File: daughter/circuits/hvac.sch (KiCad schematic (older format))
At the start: 60 parts, among them Q1 Q_MBT3904, Q10 BC846, Q11 BSS84, Q12 BSS84, Q13 Q_MBT3904, Q14 Q_MBT3904, Q15 Q_DMT3020, Q16 Q_DMT3020, Q2 Q_MBT3904, Q3 Q_DMT3020, Q4 Q_DMT3020, Q5 Q_MBT3904, Q6 Q_MBT3904, Q7 Q_DMT3020, Q8 Q_DMT3020, Q9 BC846, U10 MAX11617, U11 LTV-827S, U9 MCP23017_SS

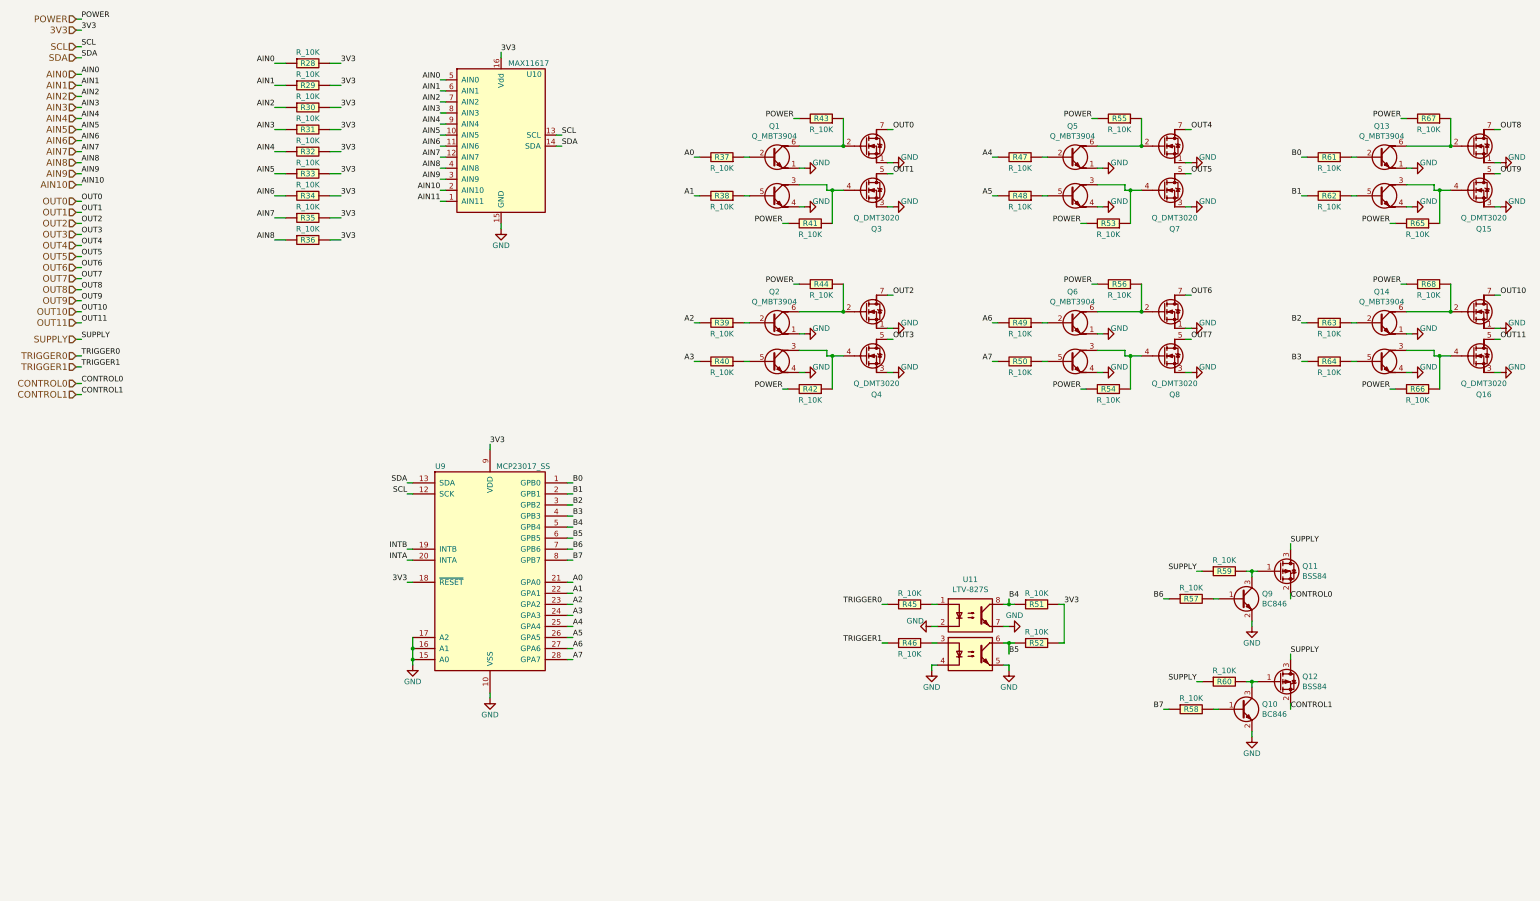
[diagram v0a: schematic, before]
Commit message: 0) Switched to h-bridge drivers for hvac 1) Connected ignition sense io 2) MCP config pins and reset 3) Fixed usb resistors 4) Fixed BJT footprint 5) Added car interface pcb for C6 Corvette
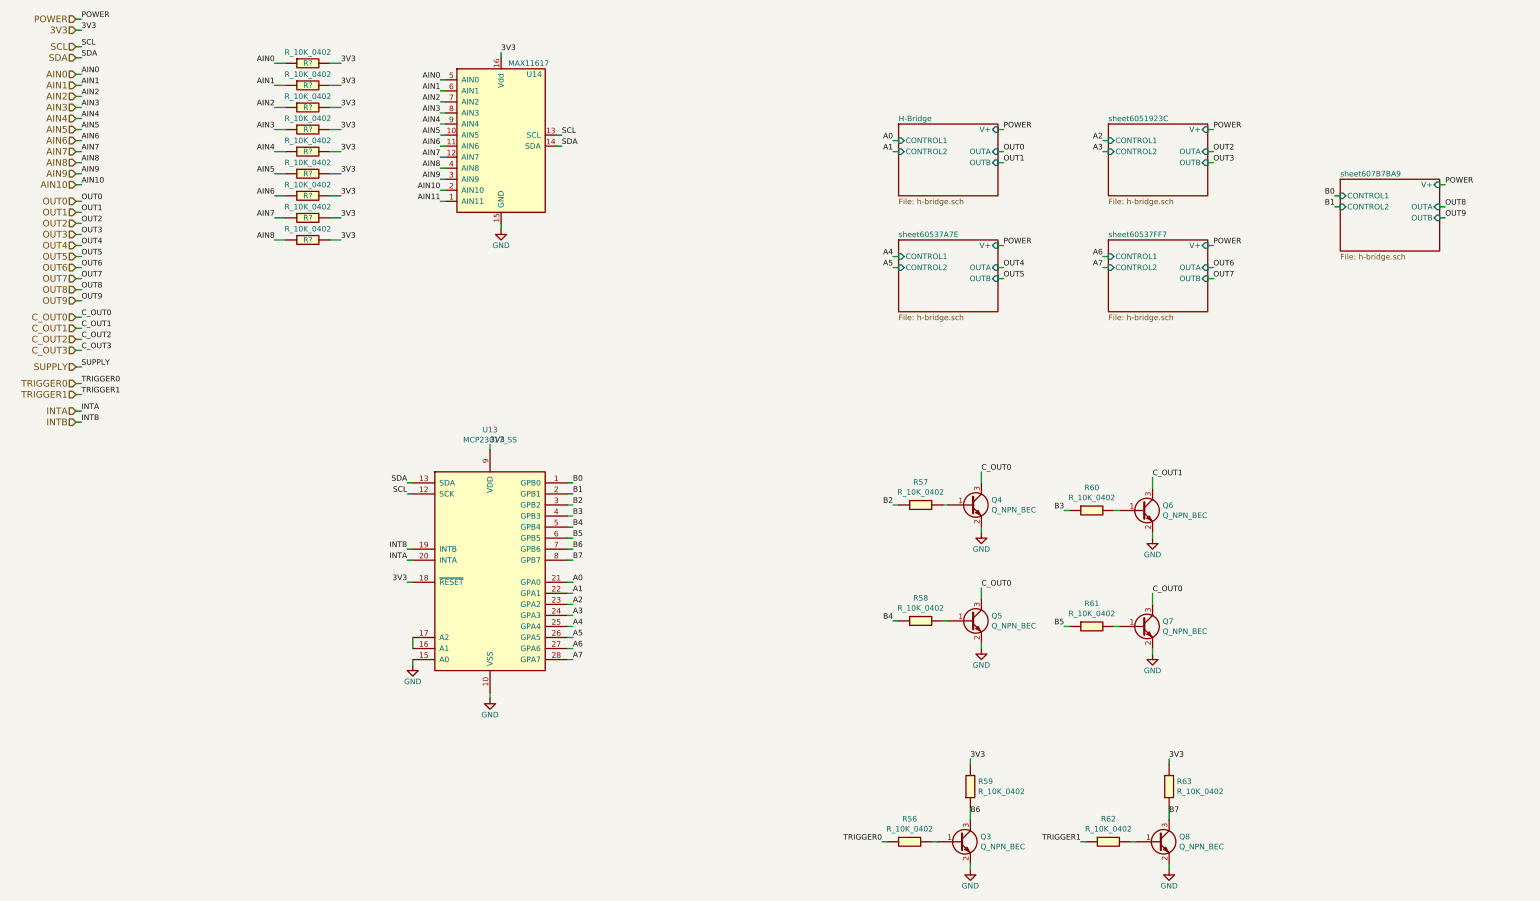
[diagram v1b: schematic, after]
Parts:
- removed Q1, Q13, Q14, Q2, Q5, Q6: Q_MBT3904, Package_TO_SOT_SMD:SOT-363_SC-70-6_Handsoldering, symbol open-dash-daughterboard-rescue:Q_MBT3904-Open_Automation
- removed Q10, Q9: BC846, Package_TO_SOT_SMD:SOT-23, symbol open-dash-daughterboard-rescue:BC846-Open_Automation
- removed Q11, Q12: BSS84, Package_TO_SOT_SMD:SOT-23, symbol open-dash-daughterboard-rescue:BSS84-Open_Automation
- removed Q15, Q16, Q3, Q4, Q7, Q8: Q_DMT3020, Package_SO:SO-8_3.9x4.9mm_P1.27mm, symbol open-dash-daughterboard-rescue:Q_DMT3020-Open_Automation
- removed R28, R29, R30, R31, R32, R33, R34, R35, R36, R37, R38, R39, R40, R41, R42, R43, R44, R45, R46, R47, R48, R49, R50, R51, R52, R53, R54, R55, R56, R57, R58, R59, R60, R61, R62, R63, R64, R65, R66, R67, R68: R_10K, Resistor_SMD:R_0603_1608Metric_Pad0.98x0.95mm_HandSolder, symbol open-dash-daughterboard-rescue:R_10K-Open_Automation
- removed U11: LTV-827S, Package_DIP:SMDIP-8_W9.53mm, symbol open-dash-daughterboard-rescue:LTV-827S-Open_Automation
- removed U9: MCP23017_SS, Package_SO:SSOP-28_5.3x10.2mm_P0.65mm, symbol open-dash-daughterboard-rescue:MCP23017_SS-Open_Automation
- added Q3, Q4, Q5, Q6, Q7, Q8: Q_NPN_BEC, Package_TO_SOT_SMD:SOT-23, symbol Open_Automation:Q_NPN_BEC
- added R56, R57, R58, R59, R60, R61, R62, R63, R? (x9): R_10K_0402, Resistor_SMD:R_0402_1005Metric_Pad0.72x0.64mm_HandSolder, symbol Open_Automation:R_10K_0402
- added U13: MCP23017_SS, Package_SO:SOIC-28W_7.5x17.9mm_P1.27mm, symbol Open_Automation:MCP23017_SS
- renumbered U10 to U14
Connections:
- net 3V3: now also R59.2, R63.2, R?.2, R?.2, R?.2, R?.2, R?.2, R?.2, R?.2, R?.2, R?.2, U13.18 (~RESET~), U13.9 (VDD)
- net A0: now also U13.21 (GPA0)
- net A1: now also U13.22 (GPA1)
- net A2: now also U13.23 (GPA2)
- net A3: now also U13.24 (GPA3)
- net A4: now also U13.25 (GPA4)
- net A5: now also U13.26 (GPA5)
- net A6: now also U13.27 (GPA6)
- net A7: now also U13.28 (GPA7)
- net AIN0: now also R?.1
- net AIN1: now also R?.1
- net AIN2: now also R?.1
- net AIN3: now also R?.1
- net AIN4: now also R?.1
- net AIN5: now also R?.1
- net AIN6: now also R?.1
- net AIN7: now also R?.1
- net AIN8: now also R?.1
- net B0: now also U13.1 (GPB0)
- net B1: now also U13.2 (GPB1)
- net B2: now also R57.1, U13.3 (GPB2)
- net B3: now also R60.1, U13.4 (GPB3)
- net B4: now also R58.1, U13.5 (GPB4)
- net B5: now also R61.1, U13.6 (GPB5)
- net B6: now also Q3.3 (C), R59.1, U13.7 (GPB6)
- net B7: now also Q8.3 (C), R63.1, U13.8 (GPB7)
- net GND: now also Q3.2 (E), Q4.2 (E), Q5.2 (E), Q6.2 (E), Q7.2 (E), Q8.2 (E), U13.10 (VSS), U13.15 (A0)
- net INTA: now also U13.20 (INTA)
- net INTB: now also U13.19 (INTB)
- net SCL: now also U13.12 (SCK)
- net SDA: now also U13.13 (SDA)
- net TRIGGER0: now also R56.1
- net TRIGGER1: now also R62.1
- new net: Q4.1 (B), R57.2
- new net: Q6.1 (B), R60.2
- new net: Q5.1 (B), R58.2
- new net: Q7.1 (B), R61.2
- new net: Q8.1 (B), R62.2
- new net: Q3.1 (B), R56.2
- new net: U13.16 (A1), U13.17 (A2)
- new net C_OUT0: Q4.3 (C), Q5.3 (C), Q7.3 (C)
- new net C_OUT1: Q6.3 (C)

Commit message: finished schematic, working on layout
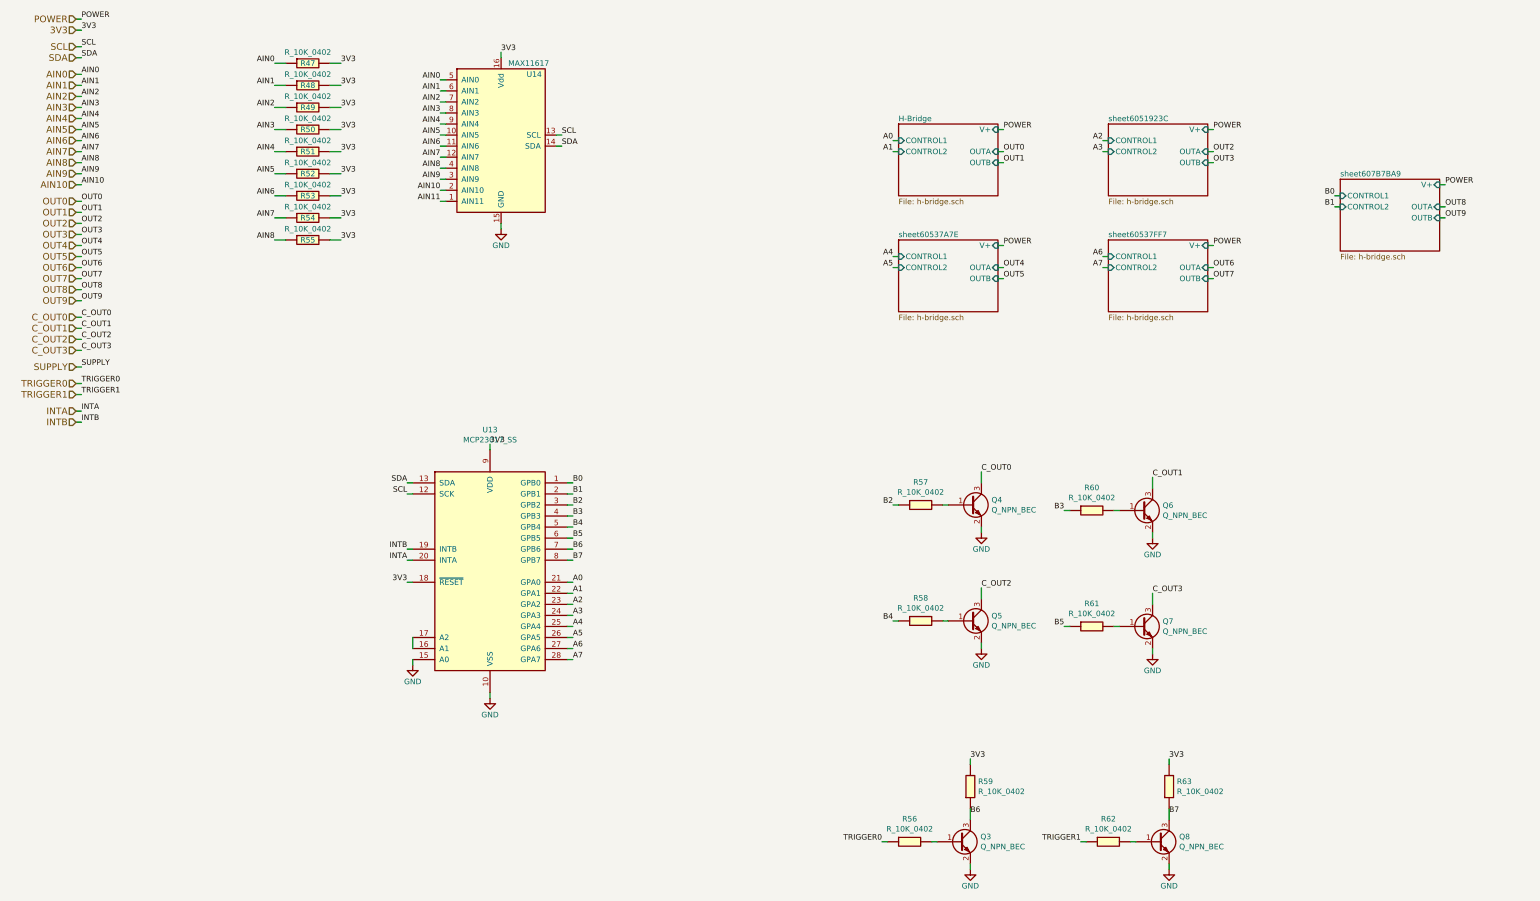
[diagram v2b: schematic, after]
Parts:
- gave numbers to parts that had none: 9
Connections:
- net C_OUT0: no longer Q5.3 (C), Q7.3 (C)
- net C_OUT2: now also Q5.3 (C)
- net C_OUT3: now also Q7.3 (C)
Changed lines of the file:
@@
 	9900 6350 9900 6450
 Text Label 9900 6350 0    50   ~ 0
-C_OUT0
+C_OUT2
 $Comp
 L Open_Automation:Q_NPN_BEC Q?
@@
 	11450 6400 11450 6500
 Text Label 11450 6400 0    50   ~ 0
-C_OUT0
+C_OUT3
 $Sheet
 S 13150 2650 900  650
@@
 AR Path="/601F213A/60537A7E/6053D306" Ref="R?"  Part="1"
 AR Path="/601F213A/60537FF7/6053D306" Ref="R?"  Part="1"
-AR Path="/601F213A/6053D306" Ref="R?"  Part="1"
-F 0 "R?" V 3800 1600 50  0000 C CNN
+AR Path="/601F213A/6053D306" Ref="R47"  Part="1"
+F 0 "R47" V 3800 1600 50  0000 C CNN
 F 1 "R_10K_0402" V 3700 1600 50  0000 C CNN
 F 2 "Resistor_SMD:R_0402_1005Metric_Pad0.72x0.64mm_HandSolder" V 3730 1600 50  0001 C CNN
@@
 AR Path="/601F213A/60537A7E/60546E01" Ref="R?"  Part="1"
 AR Path="/601F213A/60537FF7/60546E01" Ref="R?"  Part="1"
-AR Path="/601F213A/60546E01" Ref="R?"  Part="1"
-F 0 "R?" V 3800 1800 50  0000 C CNN
+AR Path="/601F213A/60546E01" Ref="R48"  Part="1"
+F 0 "R48" V 3800 1800 50  0000 C CNN
 F 1 "R_10K_0402" V 3700 1800 50  0000 C CNN
 F 2 "Resistor_SMD:R_0402_1005Metric_Pad0.72x0.64mm_HandSolder" V 3730 1800 50  0001 C CNN
@@
 AR Path="/601F213A/60537A7E/6054E653" Ref="R?"  Part="1"
 AR Path="/601F213A/60537FF7/6054E653" Ref="R?"  Part="1"
-AR Path="/601F213A/6054E653" Ref="R?"  Part="1"
-F 0 "R?" V 3800 2000 50  0000 C CNN
+AR Path="/601F213A/6054E653" Ref="R49"  Part="1"
+F 0 "R49" V 3800 2000 50  0000 C CNN
 F 1 "R_10K_0402" V 3700 2000 50  0000 C CNN
 F 2 "Resistor_SMD:R_0402_1005Metric_Pad0.72x0.64mm_HandSolder" V 3730 2000 50  0001 C CNN
@@
 AR Path="/601F213A/60537A7E/6054E65F" Ref="R?"  Part="1"
 AR Path="/601F213A/60537FF7/6054E65F" Ref="R?"  Part="1"
-AR Path="/601F213A/6054E65F" Ref="R?"  Part="1"
-F 0 "R?" V 3800 2200 50  0000 C CNN
+AR Path="/601F213A/6054E65F" Ref="R50"  Part="1"
+F 0 "R50" V 3800 2200 50  0000 C CNN
 F 1 "R_10K_0402" V 3700 2200 50  0000 C CNN
 F 2 "Resistor_SMD:R_0402_1005Metric_Pad0.72x0.64mm_HandSolder" V 3730 2200 50  0001 C CNN
@@
 AR Path="/601F213A/60537A7E/6055662E" Ref="R?"  Part="1"
 AR Path="/601F213A/60537FF7/6055662E" Ref="R?"  Part="1"
-AR Path="/601F213A/6055662E" Ref="R?"  Part="1"
-F 0 "R?" V 3800 2400 50  0000 C CNN
+AR Path="/601F213A/6055662E" Ref="R51"  Part="1"
+F 0 "R51" V 3800 2400 50  0000 C CNN
 F 1 "R_10K_0402" V 3700 2400 50  0000 C CNN
 F 2 "Resistor_SMD:R_0402_1005Metric_Pad0.72x0.64mm_HandSolder" V 3730 2400 50  0001 C CNN
@@
 AR Path="/601F213A/60537A7E/6055663A" Ref="R?"  Part="1"
 AR Path="/601F213A/60537FF7/6055663A" Ref="R?"  Part="1"
-AR Path="/601F213A/6055663A" Ref="R?"  Part="1"
-F 0 "R?" V 3800 2600 50  0000 C CNN
+AR Path="/601F213A/6055663A" Ref="R52"  Part="1"
+F 0 "R52" V 3800 2600 50  0000 C CNN
 F 1 "R_10K_0402" V 3700 2600 50  0000 C CNN
 F 2 "Resistor_SMD:R_0402_1005Metric_Pad0.72x0.64mm_HandSolder" V 3730 2600 50  0001 C CNN
@@
 AR Path="/601F213A/60537A7E/60556646" Ref="R?"  Part="1"
 AR Path="/601F213A/60537FF7/60556646" Ref="R?"  Part="1"
-AR Path="/601F213A/60556646" Ref="R?"  Part="1"
-F 0 "R?" V 3800 2800 50  0000 C CNN
+AR Path="/601F213A/60556646" Ref="R53"  Part="1"
+F 0 "R53" V 3800 2800 50  0000 C CNN
 F 1 "R_10K_0402" V 3700 2800 50  0000 C CNN
 F 2 "Resistor_SMD:R_0402_1005Metric_Pad0.72x0.64mm_HandSolder" V 3730 2800 50  0001 C CNN
@@
 AR Path="/601F213A/60537A7E/60556652" Ref="R?"  Part="1"
 AR Path="/601F213A/60537FF7/60556652" Ref="R?"  Part="1"
-AR Path="/601F213A/60556652" Ref="R?"  Part="1"
-F 0 "R?" V 3800 3000 50  0000 C CNN
+AR Path="/601F213A/60556652" Ref="R54"  Part="1"
+F 0 "R54" V 3800 3000 50  0000 C CNN
 F 1 "R_10K_0402" V 3700 3000 50  0000 C CNN
 F 2 "Resistor_SMD:R_0402_1005Metric_Pad0.72x0.64mm_HandSolder" V 3730 3000 50  0001 C CNN
@@
 AR Path="/601F213A/60537A7E/6055FBC9" Ref="R?"  Part="1"
 AR Path="/601F213A/60537FF7/6055FBC9" Ref="R?"  Part="1"
-AR Path="/601F213A/6055FBC9" Ref="R?"  Part="1"
-F 0 "R?" V 3800 3200 50  0000 C CNN
+AR Path="/601F213A/6055FBC9" Ref="R55"  Part="1"
+F 0 "R55" V 3800 3200 50  0000 C CNN
 F 1 "R_10K_0402" V 3700 3200 50  0000 C CNN
 F 2 "Resistor_SMD:R_0402_1005Metric_Pad0.72x0.64mm_HandSolder" V 3730 3200 50  0001 C CNN

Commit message: finished layout
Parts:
- added C35, C36: C_1uF, Capacitor_SMD:C_0402_1005Metric_Pad0.74x0.62mm_HandSolder, symbol Open_Automation:C_1uF
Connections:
- net 3V3: now also C35.1, C36.1
- net GND: now also U13.16 (A1), U13.17 (A2), C35.2, C36.2
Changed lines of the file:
@@
 	0    1    1    0
 $EndComp
+$Comp
+L open-dash-daughterboard-rescue:GND-power #PWR?
+U 1 1 6066934C
+P 6600 2150
+AR Path="/5A7BADDB/6066934C" Ref="#PWR?"  Part="1"
+AR Path="/6077D777/6066934C" Ref="#PWR?"  Part="1"
+AR Path="/601F213A/6066934C" Ref="#PWR0140"  Part="1"
+F 0 "#PWR0140" H 6600 1900 50  0001 C CNN
+F 1 "GND" H 6600 2000 50  0000 C CNN
+F 2 "" H 6600 2150 50  0000 C CNN
+F 3 "" H 6600 2150 50  0000 C CNN
+	1    6600 2150
+	1    0    0    -1
+$EndComp
+Wire Wire Line
+	6600 2100 6600 2150
+Wire Wire Line
+	6600 1750 6600 1800
+Text Label 6600 1750 0    50   ~ 0
+3V3
+$Comp
+L Open_Automation:C_1uF C?
+U 1 1 60669357
+P 6600 1950
+AR Path="/6077D777/60669357" Ref="C?"  Part="1"
+AR Path="/601F213A/60669357" Ref="C36"  Part="1"
+F 0 "C36" H 6715 1996 50  0000 L CNN
+F 1 "C_1uF" H 6715 1905 50  0000 L CNN
+F 2 "Capacitor_SMD:C_0402_1005Metric_Pad0.74x0.62mm_HandSolder" H 6700 2250 50  0001 C CNN
+F 3 "https://datasheet.lcsc.com/szlcsc/Samsung-Electro-Mechanics-CL05A105KA5NQNC_C52923.pdf" H 6600 1700 50  0001 C CNN
+F 4 "C52923" H 6600 2350 50  0001 C CNN "LCSC"
+F 5 "CL05A105KA5NQNC" H 6725 2150 60  0001 C CNN "Part Number"
+	1    6600 1950
+	1    0    0    -1
+$EndComp
+$Comp
+L open-dash-daughterboard-rescue:GND-power #PWR?
+U 1 1 606729E4
+P 4150 6500
+AR Path="/5A7BADDB/606729E4" Ref="#PWR?"  Part="1"
+AR Path="/6077D777/606729E4" Ref="#PWR?"  Part="1"
+AR Path="/601F213A/606729E4" Ref="#PWR0141"  Part="1"
+F 0 "#PWR0141" H 4150 6250 50  0001 C CNN
+F 1 "GND" H 4150 6350 50  0000 C CNN
+F 2 "" H 4150 6500 50  0000 C CNN
+F 3 "" H 4150 6500 50  0000 C CNN
+	1    4150 6500
+	1    0    0    -1
+$EndComp
+Wire Wire Line
+	4150 6450 4150 6500
+Wire Wire Line
+	4150 6100 4150 6150
+Text Label 4150 6100 0    50   ~ 0
+3V3
+$Comp
+L Open_Automation:C_1uF C?
+U 1 1 60672AAD
+P 4150 6300
+AR Path="/6077D777/60672AAD" Ref="C?"  Part="1"
+AR Path="/601F213A/60672AAD" Ref="C35"  Part="1"
+F 0 "C35" H 4265 6346 50  0000 L CNN
+F 1 "C_1uF" H 4265 6255 50  0000 L CNN
+F 2 "Capacitor_SMD:C_0402_1005Metric_Pad0.74x0.62mm_HandSolder" H 4250 6600 50  0001 C CNN
+F 3 "https://datasheet.lcsc.com/szlcsc/Samsung-Electro-Mechanics-CL05A105KA5NQNC_C52923.pdf" H 4150 6050 50  0001 C CNN
+F 4 "C52923" H 4150 6700 50  0001 C CNN "LCSC"
+F 5 "CL05A105KA5NQNC" H 4275 6500 60  0001 C CNN "Part Number"
+	1    4150 6300
+	1    0    0    -1
+$EndComp
+Wire Wire Line
+	4750 7000 4750 6900
+Connection ~ 4750 7000
+Connection ~ 4750 6900
 $EndSCHEMATC

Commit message: sent v1.2 to fab
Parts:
- removed C35, C36: C_1uF, Capacitor_SMD:C_0402_1005Metric_Pad0.74x0.62mm_HandSolder, symbol Open_Automation:C_1uF
- removed U14: MAX11617, Package_SO:QSOP-16_3.9x4.9mm_P0.635mm, symbol open-dash-daughterboard-rescue:MAX11617-Open_Automation
- added C35, C36, C38, C39: C_100nF_0402, Capacitor_SMD:C_0402_1005Metric_Pad0.74x0.62mm_HandSolder, symbol Open_Automation:C_100nF_0402
- added U14, U15, U16: ADC_ADS1015, Package_SO:MSOP-10_3x3mm_P0.5mm, symbol Open_Automation:ADC_ADS1015
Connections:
- net 3V3: now also C35.1, C36.1, C38.1, C39.1, U14.1 (ADDR), U14.8 (VDD), U15.8 (VDD), U16.8 (VDD)
- net AIN0: now also U15.4 (AIN0)
- net AIN1: now also U15.5 (AIN1)
- net AIN10: now also U16.6 (AIN2)
- net AIN11: now also U16.7 (AIN3)
- net AIN2: now also U15.6 (AIN2)
- net AIN3: now also U15.7 (AIN3)
- net AIN4: now also U14.4 (AIN0)
- net AIN5: now also U14.5 (AIN1)
- net AIN6: now also U14.6 (AIN2)
- net AIN7: now also U14.7 (AIN3)
- net AIN8: now also U16.4 (AIN0)
- net AIN9: now also U16.5 (AIN1)
- net GND: now also C35.2, C36.2, C38.2, C39.2, U14.3 (GND), U15.1 (ADDR), U15.3 (GND), U16.3 (GND)
- net SCL: now also U14.10 (SCL), U15.10 (SCL), U16.1 (ADDR), U16.10 (SCL)
- net SDA: now also U14.9 (SDA), U15.9 (SDA), U16.9 (SDA)
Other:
- moved on the sheet: Q3, Q4, Q5, Q6, Q7, Q8, R56, R57, R58, R59, R60, R61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
